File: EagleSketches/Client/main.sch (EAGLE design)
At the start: 15 parts

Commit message: Nye UUID's og eagle ændringer
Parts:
- added BT1: (no value), SparkFun-Batteries:BATTERY-9V
- added C1: 1mF, SparkFun-Capacitors:1000UF-RADIAL-5MM-25V-20%
- added C2: 0.1uF, SparkFun-Capacitors:0.1UF-KIT-EZ-50V-20%
- added R7: 10, SparkFun-Resistors:10OHM-HORIZ-1/4W-1%
- added U1: LM386N, SparkFun-IC-Amplifiers:LM386
- added VR2: 10k, SparkFun-Resistors:POTENTIOMETER_SLIDE-60MM-1/2W-20%
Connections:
- new net N$11: C1.+, SP1.2
- new net N$13: C1.-, C2.1, U1.OUT
- new net N$19: C2.2, R7.1
- new net N$20: R7.2
- new net N$21: U$2.IO35, VR2.S
- new net N$22: BT1.-, U1.V+
- new net N$23: U1.+IN, VR2.E
- net GND: now also BT1.+, SP1.1, U1.-IN, U1.V-, VR2.A
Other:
- moved on the sheet: VR1
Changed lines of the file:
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@@
 <layer number="56" name="wert" color="7" fill="1" visible="no" active="no"/>
 <layer number="57" name="tCAD" color="7" fill="1" visible="no" active="no"/>
+<layer number="58" name="bCopper" color="7" fill="1" visible="no" active="no"/>
 <layer number="59" name="tCarbon" color="7" fill="1" visible="no" active="no"/>
 <layer number="60" name="bCarbon" color="7" fill="1" visible="no" active="no"/>
@@
 <layer number="250" name="Descript" color="3" fill="1" visible="no" active="no"/>
 <layer number="251" name="SMDround" color="12" fill="11" visible="no" active="no"/>
+<layer number="253" name="Extra" color="7" fill="1" visible="no" active="no"/>
 <layer number="254" name="cooling" color="7" fill="1" visible="no" active="no"/>
 <layer number="255" name="routoute" color="7" fill="1" visible="no" active="no"/>
@@
 <part name="R6" library="SparkFun-Resistors" deviceset="10KOHM" device="-HORIZ-1/4W-1%" value="10k"/>
 <part name="SP1" library="buzzer" library_urn="urn:adsk.eagle:library:113" deviceset="AL11P" device="" package3d_urn="urn:adsk.eagle:package:5308/1"/>
+<part name="R7" library="SparkFun-Resistors" deviceset="10OHM" device="-HORIZ-1/4W-1%" value="10"/>
+<part name="C1" library="SparkFun-Capacitors" deviceset="1000UF" device="-RADIAL-5MM-25V-20%" value="1mF"/>
+<part name="C2" library="SparkFun-Capacitors" deviceset="0.1UF" device="-KIT-EZ-50V-20%" value="0.1uF"/>
+<part name="U1" library="SparkFun-IC-Amplifiers" deviceset="LM386" device="" value="LM386N"/>
+<part name="VR2" library="SparkFun-Resistors" deviceset="POTENTIOMETER_SLIDE" device="-60MM-1/2W-20%" value="10k"/>
+<part name="BT1" library="SparkFun-Batteries" deviceset="BATTERY" device="-9V"/>
 </parts>
 <sheets>
@@
 </plain>
 <instances>
-<instance part="VR1" gate="G$1" x="40.64" y="83.82" smashed="yes" rot="R270">
-<attribute name="NAME" x="40.386" y="80.772" size="1.778" layer="95" font="vector" rot="R180"/>
-<attribute name="VALUE" x="40.64" y="85.09" size="1.778" layer="95" font="vector" align="bottom-center"/>
+<instance part="VR1" gate="G$1" x="43.18" y="83.82" smashed="yes" rot="R270">
+<attribute name="NAME" x="42.926" y="80.772" size="1.778" layer="95" font="vector" rot="R180"/>
+<attribute name="VALUE" x="43.18" y="85.09" size="1.778" layer="95" font="vector" align="bottom-center"/>
 </instance>
 <instance part="U$1" gate="G$1" x="81.28" y="68.58" smashed="yes">
@@
 <attribute name="NAME" x="-11.43" y="135.89" size="1.778" layer="95"/>
 <attribute name="VALUE" x="-11.43" y="126.365" size="1.778" layer="96"/>
+</instance>
+<instance part="R7" gate="G$1" x="10.16" y="99.06" smashed="yes">
+<attribute name="NAME" x="10.16" y="100.584" size="1.778" layer="95" font="vector" align="bottom-center"/>
+<attribute name="VALUE" x="10.16" y="97.536" size="1.778" layer="96" font="vector" align="top-center"/>
+</instance>
+<instance part="C1" gate="G$1" x="5.08" y="124.46" smashed="yes">
+<attribute name="NAME" x="6.096" y="125.095" size="1.778" layer="95" font="vector"/>
+<attribute name="VALUE" x="6.096" y="120.269" size="1.778" layer="96" font="vector"/>
+</instance>
+<instance part="C2" gate="G$1" x="5.08" y="106.68" smashed="yes">
+<attribute name="NAME" x="6.604" y="109.601" size="1.778" layer="95" font="vector"/>
+<attribute name="VALUE" x="6.604" y="104.521" size="1.778" layer="96" font="vector"/>
+</instance>
+<instance part="U1" gate="G1" x="-22.86" y="114.3" smashed="yes">
+<attribute name="NAME" x="-15.24" y="120.142" size="1.778" layer="95" font="vector"/>
+<attribute name="VALUE" x="-15.24" y="106.68" size="1.778" layer="95" font="vector"/>
+</instance>
+<instance part="VR2" gate="G$1" x="-45.72" y="111.76" smashed="yes" rot="R270">
+<attribute name="NAME" x="-45.974" y="108.712" size="1.778" layer="95" font="vector" rot="R180"/>
+<attribute name="VALUE" x="-45.72" y="113.03" size="1.778" layer="95" font="vector" align="bottom-center"/>
+</instance>
+<instance part="BT1" gate="G$1" x="-43.18" y="134.62" smashed="yes">
+<attribute name="NAME" x="-43.18" y="138.938" size="1.778" layer="95" font="vector" align="bottom-center"/>
+<attribute name="VALUE" x="-43.18" y="130.302" size="1.778" layer="96" font="vector" align="top-center"/>
 </instance>
 </instances>
@@
 <segment>
 <pinref part="VR1" gate="G$1" pin="A"/>
-<wire x1="33.02" y1="83.82" x2="27.94" y2="83.82" width="0.1524" layer="91"/>
+<wire x1="35.56" y1="83.82" x2="27.94" y2="83.82" width="0.1524" layer="91"/>
 <label x="27.94" y="86.36" size="1.778" layer="95"/>
 </segment>
@@
 <label x="-76.2" y="78.74" size="1.778" layer="95"/>
 </segment>
+<segment>
+<pinref part="SP1" gate="G$1" pin="1"/>
+<wire x1="-12.7" y1="129.54" x2="-17.78" y2="129.54" width="0.1524" layer="91"/>
+<label x="-17.78" y="129.54" size="1.778" layer="95"/>
+</segment>
+<segment>
+<pinref part="VR2" gate="G$1" pin="A"/>
+<wire x1="-53.34" y1="111.76" x2="-55.88" y2="111.76" width="0.1524" layer="91"/>
+<label x="-55.88" y="111.76" size="1.778" layer="95"/>
+</segment>
+<segment>
+<pinref part="U1" gate="G1" pin="V-"/>
+<wire x1="-22.86" y1="106.68" x2="-22.86" y2="101.6" width="0.1524" layer="91"/>
+<label x="-22.86" y="101.6" size="1.778" layer="95"/>
+</segment>
+<segment>
+<pinref part="U1" gate="G1" pin="-IN"/>
+<wire x1="-27.94" y1="116.84" x2="-33.02" y2="116.84" width="0.1524" layer="91"/>
+<label x="-33.02" y="116.84" size="1.778" layer="95"/>
+</segment>
+<segment>
+<pinref part="BT1" gate="G$1" pin="+"/>
+<wire x1="-48.26" y1="134.62" x2="-53.34" y2="134.62" width="0.1524" layer="91"/>
+<label x="-53.34" y="134.62" size="1.778" layer="95"/>
+</segment>
 </net>
 <net name="5V" class="0">
@@
 <segment>
 <pinref part="VR1" gate="G$1" pin="S"/>
-<wire x1="40.64" y1="78.74" x2="40.64" y2="76.2" width="0.1524" layer="91"/>
+<wire x1="43.18" y1="78.74" x2="40.64" y2="76.2" width="0.1524" layer="91"/>
 <label x="40.64" y="76.2" size="1.778" layer="95"/>
 </segment>
@@
 <pinref part="U$1" gate="G$1" pin="VO"/>
 <pinref part="VR1" gate="G$1" pin="E"/>
-<wire x1="71.12" y1="83.82" x2="48.26" y2="83.82" width="0.1524" layer="91"/>
+<wire x1="71.12" y1="83.82" x2="50.8" y2="83.82" width="0.1524" layer="91"/>
 </segment>
 </net>
@@
 </segment>
 </net>
+<net name="N$11" class="0">
+<segment>
+<pinref part="SP1" gate="G$1" pin="2"/>
+<wire x1="-2.54" y1="129.54" x2="5.08" y2="129.54" width="0.1524" layer="91"/>
+<pinref part="C1" gate="G$1" pin="+"/>
+<wire x1="5.08" y1="129.54" x2="5.08" y2="127" width="0.1524" layer="91"/>
+</segment>
+</net>
+<net name="N$13" class="0">
+<segment>
+<pinref part="U1" gate="G1" pin="OUT"/>
+<pinref part="C1" gate="G$1" pin="-"/>
+<wire x1="-12.7" y1="114.3" x2="5.08" y2="114.3" width="0.1524" layer="91"/>
+<wire x1="5.08" y1="114.3" x2="5.08" y2="119.38" width="0.1524" layer="91"/>
+<pinref part="C2" gate="G$1" pin="1"/>
+<wire x1="5.08" y1="114.3" x2="5.08" y2="111.76" width="0.1524" layer="91"/>
+<junction x="5.08" y="114.3"/>
+</segment>
+</net>
+<net name="N$19" class="0">
+<segment>
+<pinref part="C2" gate="G$1" pin="2"/>
+<pinref part="R7" gate="G$1" pin="1"/>
+<wire x1="5.08" y1="104.14" x2="5.08" y2="99.06" width="0.1524" layer="91"/>
+</segment>
+</net>
+<net name="N$20" class="0">
+<segment>
+<pinref part="R7" gate="G$1" pin="2"/>
+<wire x1="15.24" y1="99.06" x2="20.32" y2="99.06" width="0.1524" layer="91"/>
+</segment>
+</net>
+<net name="N$23" class="0">
+<segment>
+<pinref part="VR2" gate="G$1" pin="E"/>
+<pinref part="U1" gate="G1" pin="+IN"/>
+<wire x1="-38.1" y1="111.76" x2="-27.94" y2="111.76" width="0.1524" layer="91"/>
+</segment>
+</net>
+<net name="N$21" class="0">
+<segment>
+<pinref part="U$2" gate="G$1" pin="IO35"/>
+<wire x1="-33.02" y1="73.66" x2="-35.56" y2="73.66" width="0.1524" layer="91"/>
+<wire x1="-35.56" y1="73.66" x2="-35.56" y2="104.14" width="0.1524" layer="91"/>
+<pinref part="VR2" gate="G$1" pin="S"/>
+<wire x1="-35.56" y1="104.14" x2="-45.72" y2="104.14" width="0.1524" layer="91"/>
+<wire x1="-45.72" y1="104.14" x2="-45.72" y2="106.68" width="0.1524" layer="91"/>
+</segment>
+</net>
+<net name="N$22" class="0">
+<segment>
+<pinref part="BT1" gate="G$1" pin="-"/>
+<wire x1="-38.1" y1="134.62" x2="-22.86" y2="134.62" width="0.1524" layer="91"/>
+<pinref part="U1" gate="G1" pin="V+"/>
+<wire x1="-22.86" y1="134.62" x2="-22.86" y2="121.92" width="0.1524" layer="91"/>
+</segment>
+</net>

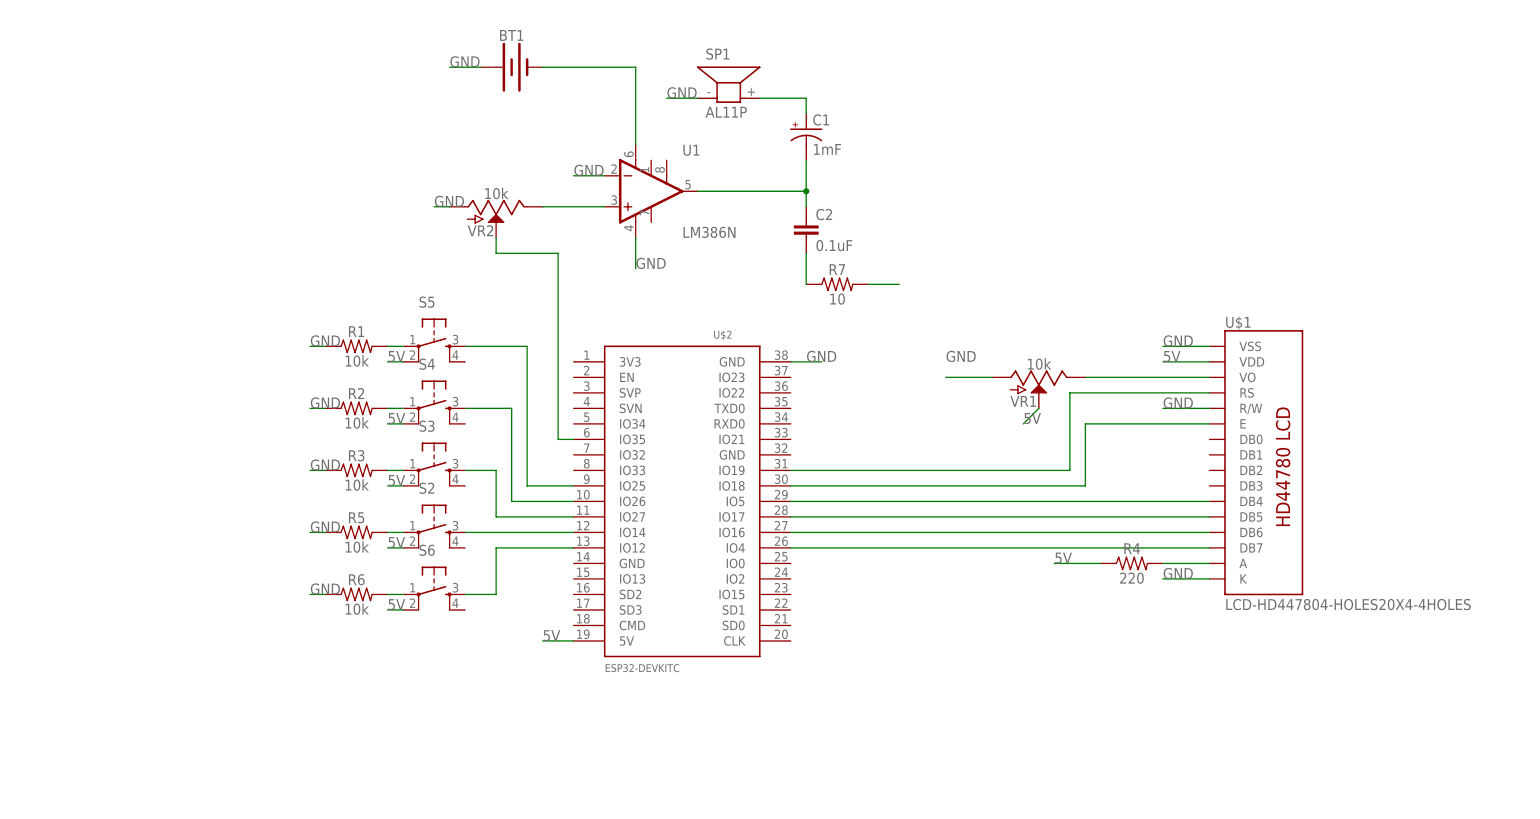
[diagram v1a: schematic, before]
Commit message: Client kode + eagle
Logging, LCD states og Eagle sketch med SD
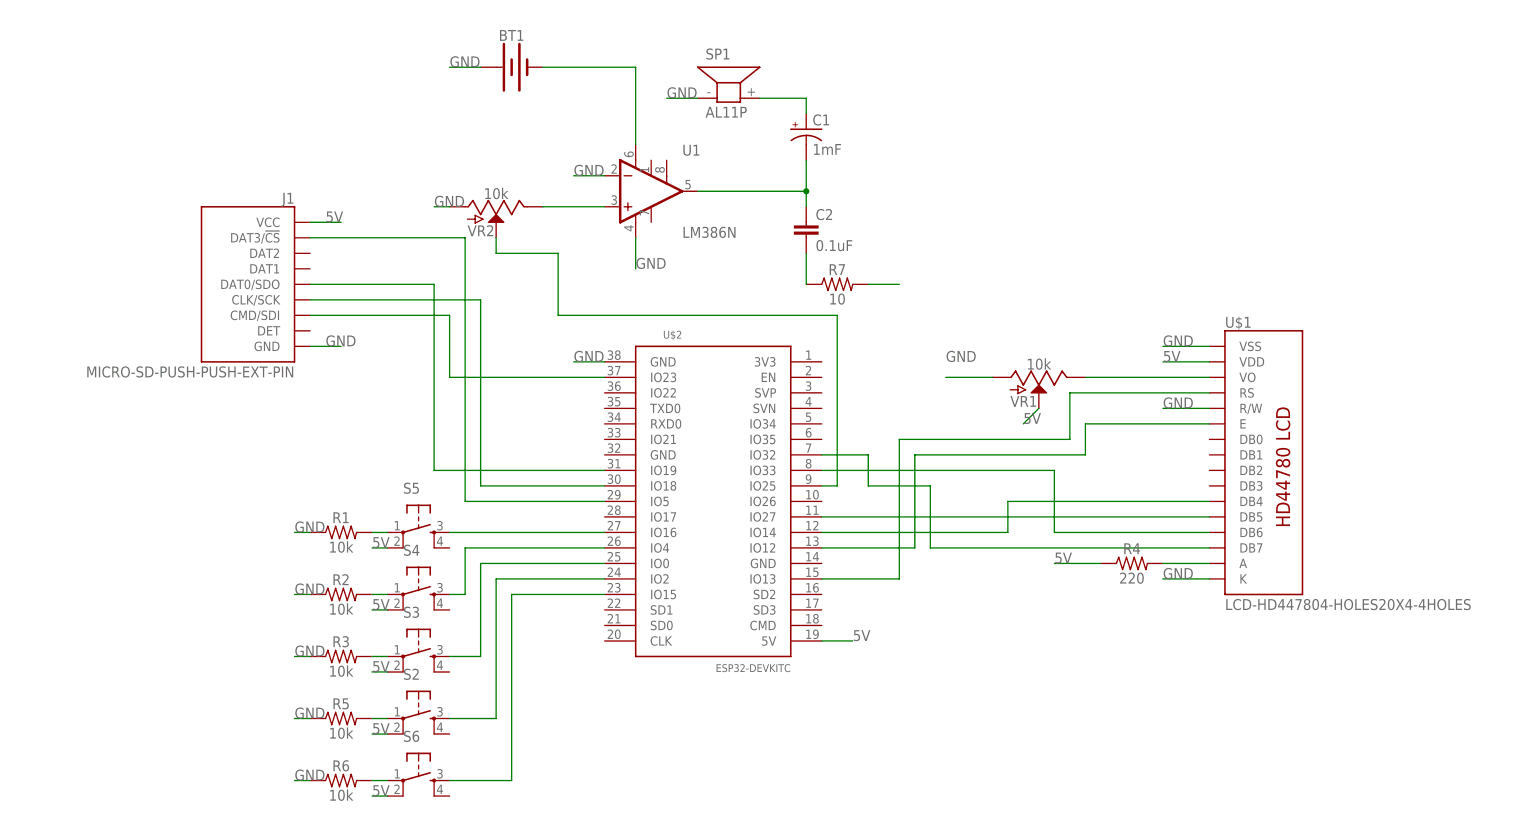
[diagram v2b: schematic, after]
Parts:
- added J1: MICRO-SD-PUSH-PUSH-EXT-PIN, SparkFun-Connectors:MICRO-SD-PUSH-PUSH-EXT-PIN
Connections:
- new net N$25: J1.DAT3/!CS!, U$2.IO5
- new net N$27: J1.CLK/SCK, U$2.IO18
- new net N$28: J1.CMD/SDI, U$2.IO23
- new net N$29: J1.DAT0/SDO, U$2.IO19
- net 5V: now also J1.VCC
- net GND: now also J1.GND
- net N$15: now also U$1.DB7, U$2.IO32; no longer S2.3, U$2.IO14
- net N$16: now also U$2.IO0; no longer U$2.IO27
- net N$17: now also U$2.IO4; no longer U$2.IO26
- net N$18: now also U$2.IO16; no longer U$2.IO25
- net N$2: now also U$2.IO13; no longer U$2.IO19
- net N$21: now also U$2.IO25; no longer U$2.IO35
- net N$3: now also U$2.IO12; no longer U$2.IO18
- net N$5: now also S2.3, U$2.IO2; no longer U$1.DB7, U$2.IO4
- net N$6: now also U$2.IO33; no longer U$2.IO16
- net N$7: now also U$1.DB4, U$2.IO14; no longer U$1.DB5, U$2.IO17
- net N$8: now also U$1.DB5, U$2.IO27; no longer U$1.DB4, U$2.IO5
- net N$9: now also U$2.IO15; no longer U$2.IO12
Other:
- moved on the sheet: R1, R2, R3, R5, R6, S2, S3, S4, S5, S6, U$2

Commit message: Working audio
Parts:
- added C3: 0.1uF, SparkFun-Capacitors:0.1UF-KIT-EZ-50V-20%
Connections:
- new net N$30: C3.2, U1.+IN
- net N$23: now also C3.1; no longer U1.+IN
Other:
- moved on the sheet: VR2
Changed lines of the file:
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@@
 <part name="BT1" library="SparkFun-Batteries" deviceset="BATTERY" device="-9V"/>
 <part name="J1" library="SparkFun-Connectors" deviceset="MICRO-SD" device="-PUSH-PUSH-EXT-PIN"/>
+<part name="C3" library="SparkFun-Capacitors" deviceset="0.1UF" device="-KIT-EZ-50V-20%" value="0.1uF"/>
 </parts>
 <sheets>
@@
 <attribute name="VALUE" x="-15.24" y="106.68" size="1.778" layer="95" font="vector"/>
 </instance>
-<instance part="VR2" gate="G$1" x="-45.72" y="111.76" smashed="yes" rot="R270">
-<attribute name="NAME" x="-45.974" y="108.712" size="1.778" layer="95" font="vector" rot="R180"/>
-<attribute name="VALUE" x="-45.72" y="113.03" size="1.778" layer="95" font="vector" align="bottom-center"/>
+<instance part="VR2" gate="G$1" x="-48.26" y="111.76" smashed="yes" rot="R270">
+<attribute name="NAME" x="-48.514" y="108.712" size="1.778" layer="95" font="vector" rot="R180"/>
+<attribute name="VALUE" x="-48.26" y="113.03" size="1.778" layer="95" font="vector" align="bottom-center"/>
 </instance>
 <instance part="BT1" gate="G$1" x="-43.18" y="134.62" smashed="yes">
@@
 <attribute name="NAME" x="-78.74" y="112.268" size="1.778" layer="95" rot="MR0"/>
 <attribute name="VALUE" x="-78.74" y="83.82" size="1.778" layer="96" rot="MR0"/>
+</instance>
+<instance part="C3" gate="G$1" x="-33.02" y="111.76" smashed="yes" rot="R90">
+<attribute name="NAME" x="-35.941" y="113.284" size="1.778" layer="95" font="vector" rot="R90"/>
+<attribute name="VALUE" x="-30.861" y="113.284" size="1.778" layer="96" font="vector" rot="R90"/>
 </instance>
 </instances>
@@
 <segment>
 <pinref part="VR2" gate="G$1" pin="A"/>
-<wire x1="-53.34" y1="111.76" x2="-55.88" y2="111.76" width="0.1524" layer="91"/>
-<label x="-55.88" y="111.76" size="1.778" layer="95"/>
+<wire x1="-55.88" y1="111.76" x2="-58.42" y2="111.76" width="0.1524" layer="91"/>
+<label x="-58.42" y="111.76" size="1.778" layer="95"/>
 </segment>
 <segment>
@@
 </segment>
 </net>
-<net name="N$23" class="0">
-<segment>
-<pinref part="VR2" gate="G$1" pin="E"/>
-<pinref part="U1" gate="G1" pin="+IN"/>
-<wire x1="-38.1" y1="111.76" x2="-27.94" y2="111.76" width="0.1524" layer="91"/>
-</segment>
-</net>
 <net name="N$21" class="0">
 <segment>
 <pinref part="VR2" gate="G$1" pin="S"/>
 <wire x1="-35.56" y1="93.98" x2="-35.56" y2="104.14" width="0.1524" layer="91"/>
-<wire x1="-35.56" y1="104.14" x2="-45.72" y2="104.14" width="0.1524" layer="91"/>
-<wire x1="-45.72" y1="104.14" x2="-45.72" y2="106.68" width="0.1524" layer="91"/>
+<wire x1="-35.56" y1="104.14" x2="-48.26" y2="104.14" width="0.1524" layer="91"/>
+<wire x1="-48.26" y1="104.14" x2="-48.26" y2="106.68" width="0.1524" layer="91"/>
 <pinref part="U$2" gate="G$1" pin="IO25"/>
 <wire x1="7.62" y1="66.04" x2="10.16" y2="66.04" width="0.1524" layer="91"/>
@@
 </segment>
 </net>
+<net name="N$23" class="0">
+<segment>
+<pinref part="VR2" gate="G$1" pin="E"/>
+<pinref part="C3" gate="G$1" pin="1"/>
+<wire x1="-40.64" y1="111.76" x2="-38.1" y2="111.76" width="0.1524" layer="91"/>
+</segment>
+</net>
+<net name="N$30" class="0">
+<segment>
+<pinref part="C3" gate="G$1" pin="2"/>
+<pinref part="U1" gate="G1" pin="+IN"/>
+<wire x1="-30.48" y1="111.76" x2="-27.94" y2="111.76" width="0.1524" layer="91"/>
+</segment>
+</net>
